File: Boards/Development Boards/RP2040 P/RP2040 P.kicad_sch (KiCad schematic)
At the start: 2 parts, among them J1 Conn_01x20_Pin, J3 Conn_01x18_Pin

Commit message: Atualização 2 RP2040 P
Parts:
- added C? (x8), C_BT? (x3), C_IN_HFI? (x6): 100n, Capacitor-0402:Capacitor_0402, symbol Device:C_Small
- added C? (x2): 470n, Capacitor-0402:Capacitor_0402, symbol Device:C_Small
- added C? (x4): 2.2u, Capacitor-0402:Capacitor_0402, symbol Device:C_Small
- added C?: 1n, symbol Device:C_Small
- added C? (x3): 1u, Capacitor-0402:Capacitor_0402, symbol Device:C_Small
- added C? (x3): 10n, Capacitor-0402:Capacitor_0402, symbol Device:C_Small
- added C?: C, Capacitor-0402:Capacitor_0402, symbol Device:C_Small
- added C? (x2): 100n, symbol Device:C_Small
- added C?: 4.7u, symbol Device:C_Small
- added C? (x4): 1u, symbol Device:C_Small
- added CR? (x4): VLMY1300-GS08, LED_VISHAY_VLMX1300_VIS, symbol VLMY1300-GS08:VLMY1300-GS08
- added C_BIAS? (x2), C_OUT?, C_VCC? (x3): 1u, Capacitor-0603:Capacitor_0603, symbol Device:C_Small
- added C_FF?: 22p, Capacitor-0402:Capacitor_0402, symbol Device:C_Small
- added C_IN-BLK? (x3): 10u, Capacitor-4mm:Capacitor_4mm, symbol Device:C_Small
- added C_IN? (x6): 4.7u, Capacitor-1206:Capacitor_1206, symbol Device:C_Small
- added C_OUT?: 100u, Capacitor-6mm:Capacitor_6mm, symbol Device:C_Small
- added C_OUT?: 560u, Capacitor-8mm:Capacitor_8mm, symbol Device:C_Small
- added C_OUT? (x6): 22u, Capacitor-0805:Capacitor_0805, symbol Device:C_Small
- added C_OUT? (x4): 10u, Capacitor-0805:Capacitor_0805, symbol Device:C_Small
- added C_OUT?: 100u, Capacitor-8mm:Capacitor_8mm, symbol Device:C_Small
- added C_OUT? (x2): 47u, Capacitor-0805:Capacitor_0805, symbol Device:C_Small
- added D? (x2): RB095BGE, RD3P175SNFRATL, symbol RB095BGE-30TL:RB095BGE-30TL
- added D?: SP3004-04XTG, SOTFL50P160X60-6N, symbol SP3004-04XTG:SP3004-04XTG
- added D? (x2): RSX301L, DIOM5026X220N, symbol RSX301L-30DDTE25:RSX301L-30DDTE25
- added D?: RB095BGE-30TL, RD3P175SNFRATL, symbol RB095BGE-30TL:RB095BGE-30TL
- added IC?: INA181A4QDCKRQ1, SOT65P210X110-6N, symbol INA181A4QDCKRQ1:INA181A4QDCKRQ1
- added IC?: NCR420ZX, SOT230P700X180-4N, symbol NCR420ZX:NCR420ZX
- added IC?: ADS1115IRUGR, ADS1115IRUGR, symbol ADS1115IRUGR:ADS1115IRUGR
- added IC?: CYPD3177-24LQXQT, QFN50P400X400X60-25N-D, symbol CYPD3177-24LQXQT:CYPD3177-24LQXQT
- added IC?: PCA9306GM,125, PCA9570GMH, symbol PCA9306GM_125:PCA9306GM,125
- added IC?: INA2181A4IDSQR, SON40P200X200X80-11N, symbol INA2181A4IDSQR:INA2181A4IDSQR
- added J?: DX07S016JA1R1500, DX07S016JA1R1500:JAE_DX07S016JA1R1500, symbol DX07S016JA1R1500:DX07S016JA1R1500
- added J? (x8): Conn_01x02_Socket, symbol Connector:Conn_01x02_Socket
- added L?: 2.2u, Inductor-10.1x10:Inductor_10.1x10, symbol Device:L
- added LED? (x2): VLMS1500-GS08, LED_00-GS08_VIS, symbol VLMS1500-GS08:VLMS1500-GS08
- added L_SW? (x2): 15u, Inductor-10.1x10:Inductor_10.1x10, symbol Device:L
- added L_SW?: 10u, Inductor-11.5x10:Inductor_11.5x10, symbol Device:L
- added Q? (x2): DMP3098LSD-13, SOIC127P600X175-8N, symbol DMP3098LSD-13:DMP3098LSD-13
- added Q? (x2): 2N7002H6327XTSA2, NMOS_2N7002:PG-SOT23-3-5_INF_MIN, symbol NMOS_2N7002:2N7002H6327XTSA2
- added Q?: BC857CMB_315, BC857CMB_315:TRANS_PMZB550UNEYL, symbol BC857CMB_315:BC857CMB_315
- added R? (x3), R_BT?: 100, Resistor-0402:RES_0402, symbol Device:R
- added R? (x2): 30k, Resistor-0402:RES_0402, symbol Device:R
- added R?: 150, Resistor-0402:RES_0402, symbol Device:R
- added R? (x2): 20K, Resistor-0402:RES_0402, symbol Device:R
- added R? (x6), R_FF?: 1k, Resistor-0402:RES_0402, symbol Device:R
- added R? (x2): 54k2, Resistor-0402:RES_0402, symbol Device:R
- added R? (x3): 370, Resistor-0402:RES_0402, symbol Device:R
- added R? (x12): 2k, Resistor-0402:RES_0402, symbol Device:R
- added R?: 10k, Resistor-0402:RES_0402, symbol Device:R
- added R?: 200k, Resistor-0402:RES_0402, symbol Device:R
- added R? (x3): 160, Resistor-0402:RES_0402, symbol Device:R
- added R?: DNP, Resistor-0402:RES_0402, symbol Device:R
- added R?: 65, Resistor-0402:RES_0402, symbol Device:R
- added R? (x2): 50k, symbol Device:R
- added R?: 95, Resistor-0402:RES_0402, symbol Device:R
- added R? (x2): 500, Resistor-0402:RES_0402, symbol Device:R
- added R? (x3): 10K, Resistor-0402:RES_0402, symbol Device:R
- added R?: PTS060301B100RP100, RESC1508X55N, symbol PTS060301B100RP100:PTS060301B100RP100
- added R?: 10k, symbol Device:R
- added R?: 320, Resistor-0402:RES_0402, symbol Device:R
- added R?: 120, Resistor-0402:RES_0402, symbol Device:R
- added R_BIAS? (x2): 5, Resistor-0402:RES_0402, symbol Device:R
- added R_BT? (x2): 50, Resistor-0402:RES_0402, symbol Device:R
- added R_ENB?: 100k, Resistor-0603:RES_0603, symbol Device:R
- added R_ENB?: 63k4, Resistor-0402:RES_0402, symbol Device:R
- added R_ENB?: 45k3, Resistor-0402:RES_0402, symbol Device:R
- added R_ENT?: 590k, Resistor-0402:RES_0402, symbol Device:R
- added R_ENT?: 931k, Resistor-0603:RES_0603, symbol Device:R
- added R_ENT?: 422k, Resistor-0402:RES_0402, symbol Device:R
- added R_FBB?: 12k6, Resistor-0603:RES_0603, symbol Device:R
- added R_FBB?: 50, Resistor-0603:RES_0603, symbol Device:R
- added R_FBB?: 8k66, Resistor-0603:RES_0603, symbol Device:R
- added R_FBB?: 120, Resistor-0603:RES_0603, symbol Device:R
- added R_FBB?: 30, Resistor-0603:RES_0603, symbol Device:R
- added R_FBB?: 22k1, Resistor-0603:RES_0603, symbol Device:R
- added R_FBT? (x3), R_PG? (x3): 100K, Resistor-0603:RES_0603, symbol Device:R
- added R_RT? (x3): 33k2, Resistor-0603:RES_0603, symbol Device:R
- added Rsense? (x2): 2.5m, symbol Device:R
- added Rsense?: 7.5m, symbol Device:R
- added U? (x3): LM61460AASQRJRRQ1, VQFN-HR14_RJR_TEX, symbol DCDC_LM61460:LM61460AASQRJRRQ1
- added U?: IRLZ44NPBF, NMOS IRLZ44:PG-TO220-3_INF, symbol NMOS IRLZ44:IRLZ44NPBF
- added U?: MAX31856MUD+T, Thermocouple:21-0066J_14_MXM, symbol MAX31856MUD-T:MAX31856MUD+T
- added U?: MAX485CSA+T, RS Transceiver:21-0041-3-M_90-0096-8L_MXM, symbol RS_Transceiver:MAX485CSA+T
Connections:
- net GND: now also C?.1, C?.1, C?.2, C?.2, C?.2, C?.2, C?.2, C?.2, C?.2, C?.2, C?.2, C?.2, C?.2, C?.2, C?.2, C?.2, C?.2, C?.2, C?.2, C?.2, C?.2, C?.2, C?.2, C?.2, C?.2, C?.2, C_BIAS?.2, C_BIAS?.2, C_IN-BLK?.2, C_IN-BLK?.2, C_IN-BLK?.2, C_IN?.2, C_IN?.2, C_IN?.2, C_IN?.2, C_IN?.2, C_IN?.2, C_IN_HFI?.2, C_IN_HFI?.2, C_IN_HFI?.2, C_IN_HFI?.2, C_IN_HFI?.2, C_IN_HFI?.2, C_OUT?.2, C_OUT?.2, C_OUT?.2, C_OUT?.2, C_OUT?.2, C_OUT?.2, C_OUT?.2, C_OUT?.2, C_OUT?.2, C_OUT?.2, C_OUT?.2, C_OUT?.2, C_OUT?.2, C_OUT?.2, C_OUT?.2, C_OUT?.2, C_VCC?.2, C_VCC?.2, C_VCC?.2, D?.2 (GND), IC?.1 (ADDR), IC?.1 (GND), IC?.11 (GND_2), IC?.19 (GND), IC?.2 (GND), IC?.22 (VSS), IC?.25 (EP), IC?.3 (GND), IC?.3 (GND), IC?.4 (GND_1), IC?.7 (AIN3), J?.1 (GND), J?.1 (Pin_1), J?.12 (GND), Q?.3, R?.1, R?.1, R?.1, R?.1, R?.1, R?.1, R?.1, R?.1, R?.2, R?.2, R?.2, R?.2, R?.2, R?.2, R_ENB?.1, R_ENB?.1, R_ENB?.1, R_FBB?.1, R_FBB?.1, R_FBB?.1, R_RT?.1, R_RT?.1, R_RT?.1, U?.1 (AGND), U?.1 (BIAS), U?.11 (PGND2), U?.11 (PGND2), U?.11 (PGND2), U?.14 (DGND), U?.3 (AGND), U?.3 (AGND), U?.3 (AGND), U?.3 (S), U?.5 (GND), U?.9 (PGND1), U?.9 (PGND1), U?.9 (PGND1)
- new net: C_OUT?.1, C_OUT?.1, C_OUT?.1, C_OUT?.1, C_OUT?.1, C_OUT?.1, D?.1, D?.3, L_SW?.2, R_FBT?.1
- new net: C?.1, R?.1, U?.4 (T+)
- new net: C?.1, C?.2, R?.1, U?.3 (T-)
- new net: IC?.1 (REF), R?.1, R?.2
- new net: IC?.6 (OUT), R?.1
- new net: D?.1 (K), Q?.1 (S1), Q?.3 (S2), R?.1
- new net: C?.2, C?.2, D?.2 (A), Q?.2 (G1), Q?.4 (G2), R?.2, R?.2, R?.2
- new net: C?.1, C?.1, IC?.18 (VBUS_IN), J?.11 (VBUS), J?.2 (VBUS), Q?.5 (D2), Q?.6 (D2), R?.1
- new net: C_BIAS?.1, R_BIAS?.1, U?.1 (BIAS) (x2)
- new net: D?.1 (IO1), IC?.15 (CC1), J?.3 (CC1)
- new net: D?.4 (IO3), IC?.14 (CC2), J?.9 (CC2)
- new net: J?.S1 (SHIELD), J?.S2 (SHIELD), J?.S3 (SHIELD), J?.S4 (SHIELD), J?.S5 (SHIELD), J?.S6 (SHIELD)
- new net: C_OUT?.1, C_OUT?.1, C_OUT?.1, C_OUT?.1, C_OUT?.1, D?.2 (A), L_SW?.2, R_BIAS?.2, R_FBT?.1, R_FF?.1
- new net: CR?.1, R?.2 (x4)
- new net: R_RT?.2, U?.6 (RT) (x3)
- new net: IC?.3 (VBUS_FET_EN), R?.1
- new net: R_ENB?.2, R_ENT?.1, U?.7 (EN/SYNC) (x3)
- new net: Q?.1 (S1), Q?.3 (S2)
- new net: Q?.2 (G1), Q?.4 (G2), R?.2, R?.2
- new net: Q?.7 (D1), Q?.8 (D1), R?.1
- new net: IC?.5 (REF1), IC?.6 (REF2), R?.1, R?.2
- new net: C_BT?.1, L_SW?.1, U?.10 (SW) (x3)
- new net: R_BT?.2, U?.13 (RBOOT) (x3)
- new net: C_BT?.2, R_BT?.1, U?.14 (CBOOT) (x3)
- new net: R_FBB?.1, R_FBT?.2, U?.4 (FB) (x2)
- new net: C_OUT?.1, C_OUT?.1, C_OUT?.1, C_OUT?.1, C_OUT?.1, D?.1, D?.3, L_SW?.2, R_BIAS?.2, R_FBT?.1
- new net: C?.1, IC?.7 (VREF2), IC?.8 (EN), R?.1
- new net: IC?.1 (OUT1), R?.1
- new net: LED?.1, R?.2
- new net: IC?.6 (ISNK_FINE), R?.1, R?.1
- new net: IC?.5 (SDA2), IC?.9 (SDA), R?.2
- new net: IC?.10 (FLIP), R?.2
- new net: IC?.10 (SCL), IC?.6 (SCL2), R?.2
- new net: R_FBB?.2, R_FBB?.2 (x3)
- new net: IC?.2 (REXT), R?.1
- new net: C?.1, IC?.24 (VCCD)
- new net: IC?.2 (VBUS_MAX), R?.2, R?.2
- new net: IC?.1 (VEN), IC?.9 (FAULT)
- new net: IC?.4 (IOUT), LED?.1
- new net: IC?.2 (ALERT/RDY), Q?.3 (D), R?.2
- new net: Q?.2, R?.1
- new net: IC?.4 (SAFE_PWR_EN), R?.1
- new net: IC?.1 (VBUS_MIN), R?.1, R?.2
- new net: IC?.9 (OUT2), R?.1
- new net: C_FF?.1, R_FF?.2
- new net: C_FF?.2, R_FBB?.1, R_FBT?.2, U?.4 (FB)
- new net +12V: CR?.2, D?.2, IC?.2 (IN-1), J?.1 (Pin_1), Rsense?.2
- new net +3.3V: C?.1, C?.1, C?.1, C?.1, C?.1, C?.2, C?.2, CR?.2, IC?.10 (VS), IC?.2 (VREF1), IC?.23 (VDDD), IC?.3 (VS), IC?.5 (ISNK_COARSE), Q?.1 (G), Q?.1 (G), R?.1, R?.1, R?.1, R?.1, R?.1, R?.1, R?.1, R?.1, R?.2, R?.2, R?.2, R?.2, R?.2, R?.2, R?.2, U?.5 (AVDD), U?.8 (DVDD)
- new net +5V: C?.1, C?.1, CR?.2, D?.5 (VCC), IC?.5 (IN-), IC?.8 (VDD), LED?.2, LED?.2, Q?.5 (D2), Q?.6 (D2), R?.1, R?.1, R?.1, R?.1, R?.1, R?.2, Rsense?.2, U?.8 (VCC)
- new net +8.4V: CR?.2, IC?.8 (IN-2), J?.2 (Pin_2), Rsense?.2
- new net 12V_Sense: C?.1, R?.2
- new net 5V_Sense: C?.1, R?.2
- new net 8.4V_Sense: C?.1, R?.2
- new net ADC RDY: C?.1, Q?.2 (S), R?.2
- new net AIN0: C?.1, IC?.4 (AIN0), R?.2
- new net AIN1: C?.1, IC?.5 (AIN1), R?.2
- new net AIN2: C?.1, IC?.6 (AIN2), R?.2
- new net DC.DC1 PGOOD: R_PG?.2, U?.5 (PGOOD)
- new net DC.DC1 VCC: C_VCC?.1, R_PG?.1, U?.2 (VCC)
- new net DC.DC2 PGOOD: R_PG?.2, U?.5 (PGOOD)
- new net DC.DC2 VCC: C_VCC?.1, R_PG?.1, U?.2 (VCC)
- new net DC.DC3 PGOOD: R_PG?.2, U?.5 (PGOOD)
- new net DC.DC3 VCC: C_VCC?.1, R_PG?.1, U?.2 (VCC)
- new net I_Sense1+: D?.2, IC?.3 (IN+1), Rsense?.1
- new net I_Sense2+: D?.2, IC?.7 (IN+2), Rsense?.1
- new net I_Sense3+: D?.1 (K), IC?.4 (IN+), Rsense?.1
- new net Main Valve Drive: J?.1 (Pin_1), Q?.3 (D), R?.2
- new net Main Valve PWM: Q?.2 (S), R?.2
- new net PRESS_SENSE: J?.2 (Pin_2), R?.1
- new net Purge Valve Drive: D?.1, D?.3, J?.2 (Pin_2), U?.2
- new net Purge Valve Enable: R?.1, U?.1 (G)
- new net RS_A: J?.1 (Pin_1), R?.2, R?.2, U?.6 (A)
- new net RS_B: J?.2 (Pin_2), R?.1, R?.1, U?.7 (B)
- new net RS_ENABLE: R?.2, U?.2 (*RE), U?.3 (DE)
- new net RS_RX: R?.2, U?.1 (RO)
- new net RS_TX: R?.1, U?.4 (DI)
- new net SCL I2C: IC?.3 (SCL1)
- new net SDA I2C: IC?.12 (HPI_SDA), IC?.4 (SDA1), R?.1
- new net SDL I2C: IC?.13 (HPI_SCL), R?.1
- new net SPI_MISO: U?.11 (SDO)
- new net SPI_MOSI: U?.12 (SDI)
- new net SPI_SCK: U?.10 (SCK)
- new net TEMP SENSE +: R?.1, R?.2, R?.2
- new net TEMP SENSE -: R?.1, R?.1, R?.1
- new net THERMO1 T+: J?.2 (Pin_2), R?.2
- new net THERMO1 T-: J?.1 (Pin_1), R?.2, U?.2 (BIAS)
- new net THERMO1_~{CS}: U?.9 (~{CS})
- new net THERMO1_~{DRDY}: U?.7 (~{DRDY})
- new net THERMO1_~{FAULT}: Q?.1, U?.13 (~{FAULT})
- new net THERMO2 T+: J?.2 (Pin_2)
- new net THERMO2 T-: J?.1 (Pin_1)
- new net THERMO3 T+: J?.2 (Pin_2)
- new net THERMO3 T-: J?.1 (Pin_1)
- new net USB-C PD ~{INT}: IC?.7 (HPI_INT)
- new net USB_DM: D?.3 (IO2), J?.5 (D-), J?.8 (D-)
- new net USB_DP: D?.6 (IO4), J?.6 (D+), J?.7 (D+)
- new net VBAT: C?.1, C?.1, C?.1, IC?.11 (VDC_OUT), J?.2 (Pin_2), L?.1, Q?.7 (D1), Q?.8 (D1)
- new net VBUS: C?.1, C?.1, C?.1, C?.1, C_IN-BLK?.1, C_IN-BLK?.1, C_IN-BLK?.1, C_IN?.1, C_IN?.1, C_IN?.1, C_IN?.1, C_IN?.1, C_IN?.1, C_IN_HFI?.1, C_IN_HFI?.1, C_IN_HFI?.1, C_IN_HFI?.1, C_IN_HFI?.1, C_IN_HFI?.1, L?.2, R_ENT?.2, R_ENT?.2, R_ENT?.2, U?.12 (VIN2), U?.12 (VIN2), U?.12 (VIN2), U?.8 (VIN1), U?.8 (VIN1), U?.8 (VIN1)
- no-connect marks 0 -> 8
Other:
- added sheet RP2040 Standard (RP2040 Standard Design.kicad_sch)
- note added: "4 Channel ESD Diode"
- note added: ">15V to 12V Converter"
- note added: ">15V to 5V Converter"
- note added: ">15V to 8.4V Converter"
- note added: "ADC + I2C Translator"
- note added: "Anti-Aliasing Filter: Fs = 860Hz => Fc = 430Hz"
- note added: "Buck Converters"
- note added: "C_IN-BLK1 and C_OUT6 are electrolytic polarized capacitors! All others are ceramic X7R capacitors with appropriate voltage ratings."
- note added: "C_IN-BLK2 and C_OUT10 are electrolytic polarized capacitors! All others are ceramic X7R capacitors with appropriate voltage ratings."
- note added: "C_IN-BLK3 and C_OUT15 are electrolytic polarized capacitors! All others are ceramic X7R capacitors with appropriate voltage ratings."
- note added: "Capacitor to adjust signal"
- note added: "Current Sensor"
- note added: "DC.DC1 VCC coloca PGOOD a 3.3V"
- note added: "DC.DC2 VCC coloca PGOOD a 3.3V"
- note added: "DC.DC3 VCC coloca PGOOD a 3.3V"
- note added: "EMI Filter"
- note added: "I/O Connectors"
- note added: "I2C ADDR is 0x08"
- note added: "I2C Fast Mode should be set around 400kHz. USB-C PD I2C ADDR is 0x08. ADS1115 I2C ADDR is 0x90. Higher frequencies may sink too much current. The total current sunk by the RP2040 in all GPIOs must be below 50mA"
- note added: "LEDs Drivers"
- note added: "Main Valve Driver"
- note added: "PNP LED Driver"
- note added: "POWER"
- note added: "Purge Valve Driver"
- note added: "RP2040 Connections"
- note added: "RS Transceiver"
- note added: "STATUS"
- note added: "THERMO FAULT"
- note added: "Tem de se escolher contactos apropriados para os termocouples!"
- note added: "Temperature Sensor"
- note added: "Temporarily assign PicoSocket as footprint. After layout design select adequate connectors."
- note added: "Thermocouple"
- note added: "Thermocouples - 3 Differential Connections (6) - INPUTs -> To Type-K probes RS485 Transceiver - 1 Differential Connection (2) - INPUT/OUTPUT Purge Valve Drive - 1 Connection - INPUT Main Valve PWM Signal Control - 1 Connection - OUTPUT Pressure Sensor Signal Input - 1 Connection - INPUT 8.4V Power Line - 1 Connection - Power Input -> Servo Motors 12V Power Line - 1 Connection - Power Input -> Pre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"
- note added: "This ADC is to be set at max sampling rate (860Hz) With AIN0 and AIN1 on differential mode and AIN2 in single-ended mode. With ADDR to ground the ADC is configured for a 0x90 I2C address"
- note added: "USB-C Power Delivery Controller (15V 5A)"
- note added: "VBUS: 16V nominal when powered by battery VBUS: 15V nominal when powered through USB-C PD"
- note added: "VMAX= 3V3/2 => 15V VMIN= 3V3/2 => 15V ICoarse = 3V3 => 5A Ifine = 0A"
- note added: "Valve Drivers"
- note added: "Verificar valores de resistências nos PMOS"
- note added: "Vout = 15V => to DC.DC Stage Iout.max = 4A"
- note added: "Vout = 15V => to LDO Iout.max = 900mA"
- note added: "Vout is set to 12.5V to compensate Diode and Rsense drops. The Schottky diode has a 425mV forward voltage drop."
- note added: "Vout is set to 5.5V to compensate Diode and Rsense drops The Schottky diode has a 420mV forward voltage drop."
- note added: "Vout is set to 5.5V to compensate Diode and Rsense drops. The Schottky diode has a 425mV forward voltage drop."
- note added: "differential routing"
- moved on the sheet: J1, J3

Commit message: Atualização 4
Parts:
- removed J1: Conn_01x20_Pin, symbol Connector:Conn_01x20_Pin
- removed J3: Conn_01x18_Pin, symbol Connector:Conn_01x18_Pin
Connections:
- net DC.DC2 PGOOD: now also C_BIAS?.2
- net DC.DC3 PGOOD: now also C_BIAS?.2
- net GND: no longer C_BIAS?.2, C_BIAS?.2
- net SDA I2C: no longer IC?.12 (HPI_SDA), R?.1
- net SDL I2C renamed SDL I2C0
- net THERMO2 T+: no longer names the net of J?.2 (Pin_2)
- net THERMO2 T-: no longer names the net of J?.1 (Pin_1)
- net THERMO3 T+: no longer names the net of J?.2 (Pin_2)
- net THERMO3 T-: no longer names the net of J?.1 (Pin_1)
- new net SDA I2C0: IC?.12 (HPI_SDA), R?.1
- no-connect marks 8 -> 11
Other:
- removed sheet RP2040 Power
- sheet RP2040 Standard ports: added GP12/I2C0 ~{SDA}, GP13/I2C0 ~{SCL}, GP29/USB VBUS EN; removed GP13/SPI1 ~{CS}, GP29/SPI1 ~{CS}, GPIO12
- note removed: "RP2040 Power"
- moved on the sheet: C?, CR?, C_BIAS?, C_BT?, C_FF?, C_IN-BLK?, C_IN?, C_IN_HFI?, C_OUT?, C_VCC?, D?, IC?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

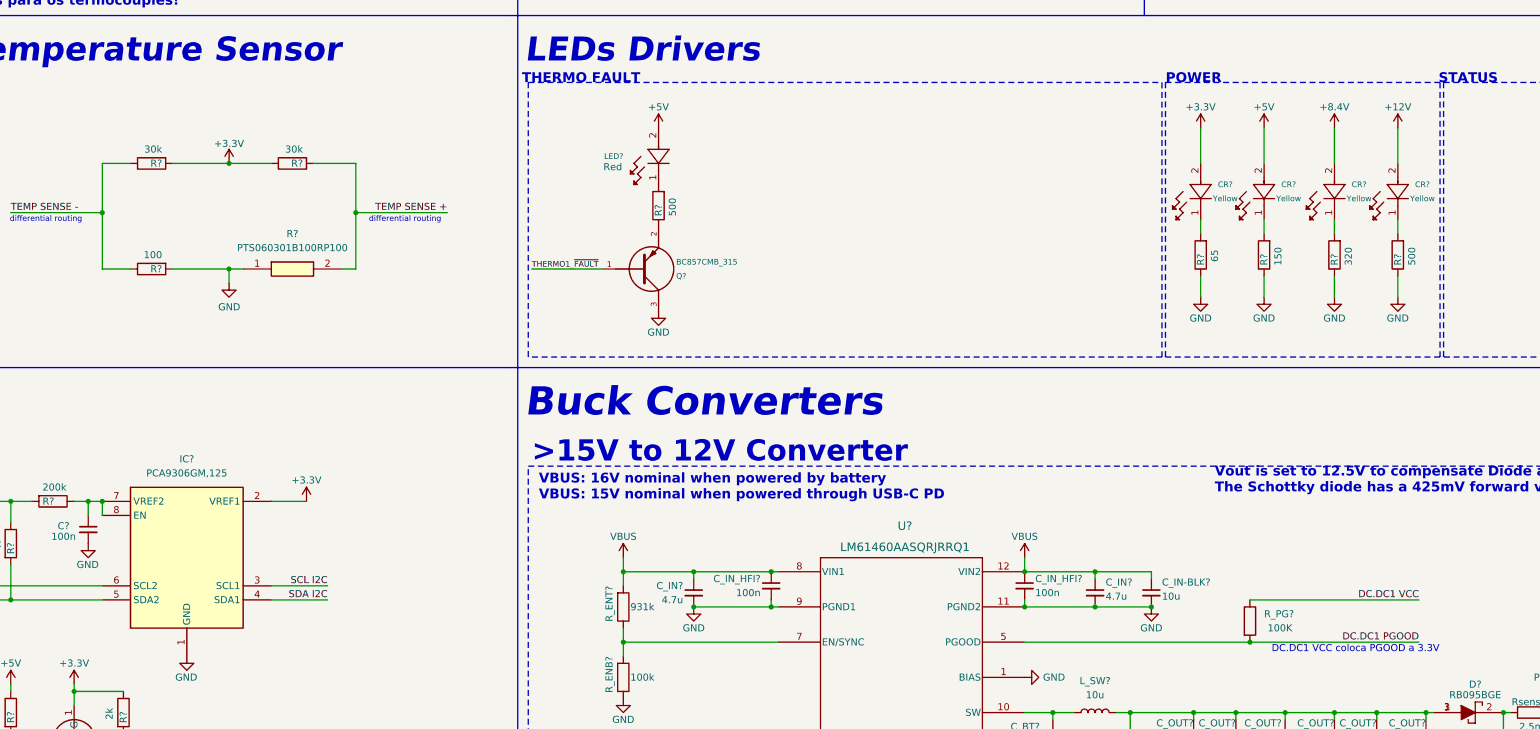
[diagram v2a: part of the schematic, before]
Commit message: Atualização RP2040 P
Copiei da TVCS Top;
Alterei conexões no microcontrolador;
Tentei pôr o Potenciómetro;
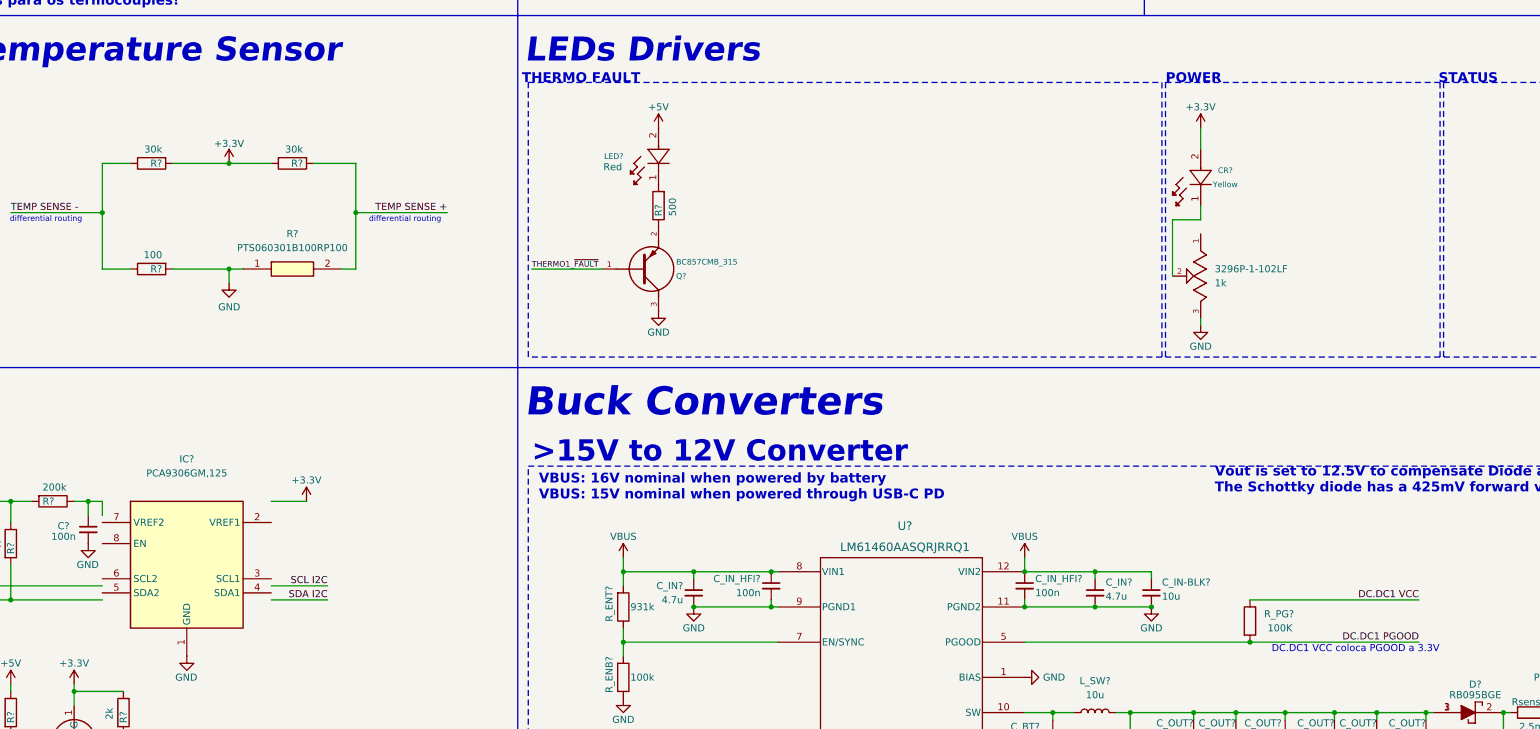
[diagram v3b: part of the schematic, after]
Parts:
- removed CR? (x3): VLMY1300-GS08, LED_VISHAY_VLMX1300_VIS, symbol VLMY1300-GS08:VLMY1300-GS08
- removed R?: 150, Resistor-0402:RES_0402, symbol Device:R
- removed R?: 65, Resistor-0402:RES_0402, symbol Device:R
- removed R?: 500, Resistor-0402:RES_0402, symbol Device:R
- removed R?: 320, Resistor-0402:RES_0402, symbol Device:R
- added 3296P-1-102LF: 1k, Pot_1k:Pot_1k, symbol Pot_1k:3296P-1-102LF
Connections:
- net +3.3V: no longer IC?.2 (VREF1)
- net GND: now also 3296P-1-102LF.3
- net SCL I2C: no longer IC?.3 (SCL1)
- net SDA I2C: no longer IC?.4 (SDA1)
- net at C?.1, R?.1: no longer IC?.7 (VREF2), IC?.8 (EN)
- net at IC?.9 (SDA), R?.2: no longer IC?.5 (SDA2)
- net at CR?.1: now also 3296P-1-102LF.2
- net at IC?.10 (SCL), R?.2: no longer IC?.6 (SCL2)
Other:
- moved on the sheet: CR?, IC?
